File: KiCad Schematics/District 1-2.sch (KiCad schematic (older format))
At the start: 23 parts, among them M1 Fan

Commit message: Updated schematic
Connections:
- net labels removed: Programming_Track
- wire segments 138 -> 136
- no-connect marks 5 -> 7
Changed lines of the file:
@@
 $Descr USLetter 11000 8500
 encoding utf-8
-Sheet 5 6
+Sheet 5 7
 Title "District 1 Power Box"
 Date "2016-09-30"
@@
 	2020 4820 2020 4740
 Wire Wire Line
-	1360 4740 2020 4740
-Wire Wire Line
-	1360 3220 1360 4740
+	2020 4740 1360 4740
+Wire Wire Line
+	1360 4740 1360 3220
 Wire Wire Line
 	2020 6330 2020 6270
@@
 	5660 2010 5660 2560
 Wire Wire Line
-	2500 3490 2500 3160
-Wire Wire Line
-	2700 3160 2700 3490
-Wire Wire Line
 	2600 3490 2600 3230
 Wire Wire Line
 	2600 3230 1800 3230
 Connection ~ 1800 3230
-Entry Wire Line
-	2500 3160 2600 3060
-Entry Wire Line
-	2700 3160 2800 3060
-Text Label 3020 3060 0    60   ~ 0
-Programming_Track
-Wire Bus Line
-	2600 3060 3910 3060
+NoConn ~ 2700 3490
+NoConn ~ 2500 3490
 $EndSCHEMATC

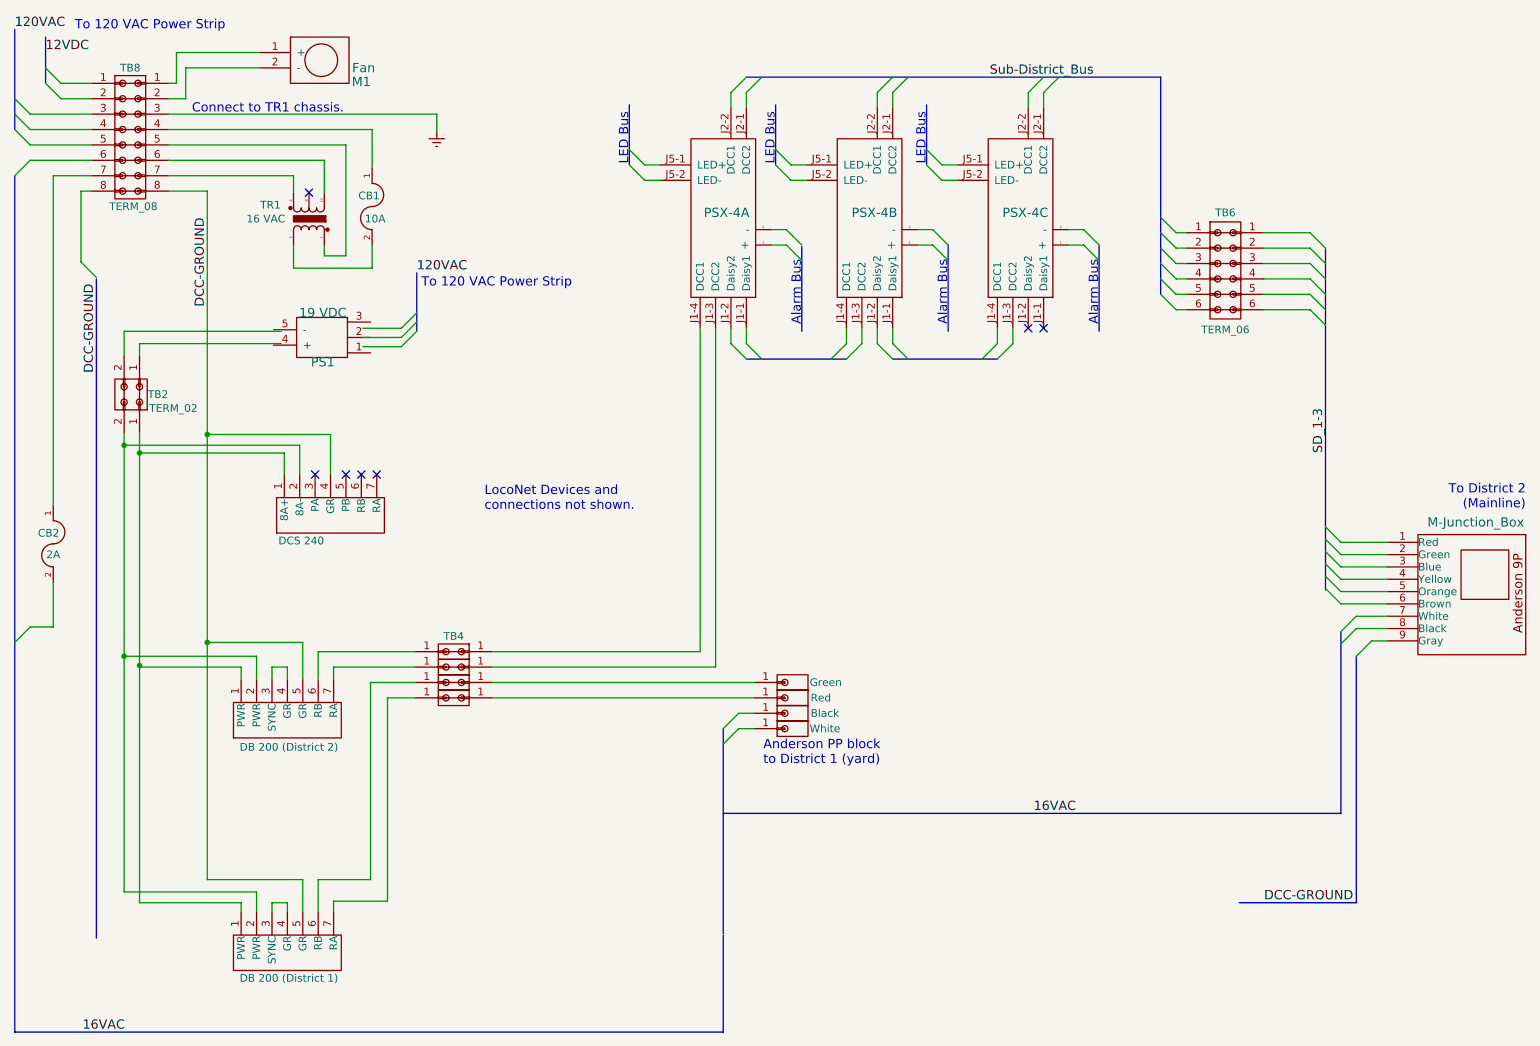
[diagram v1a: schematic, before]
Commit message: Simplified schematic
Added heirarchy sheets to simplify the schematic.
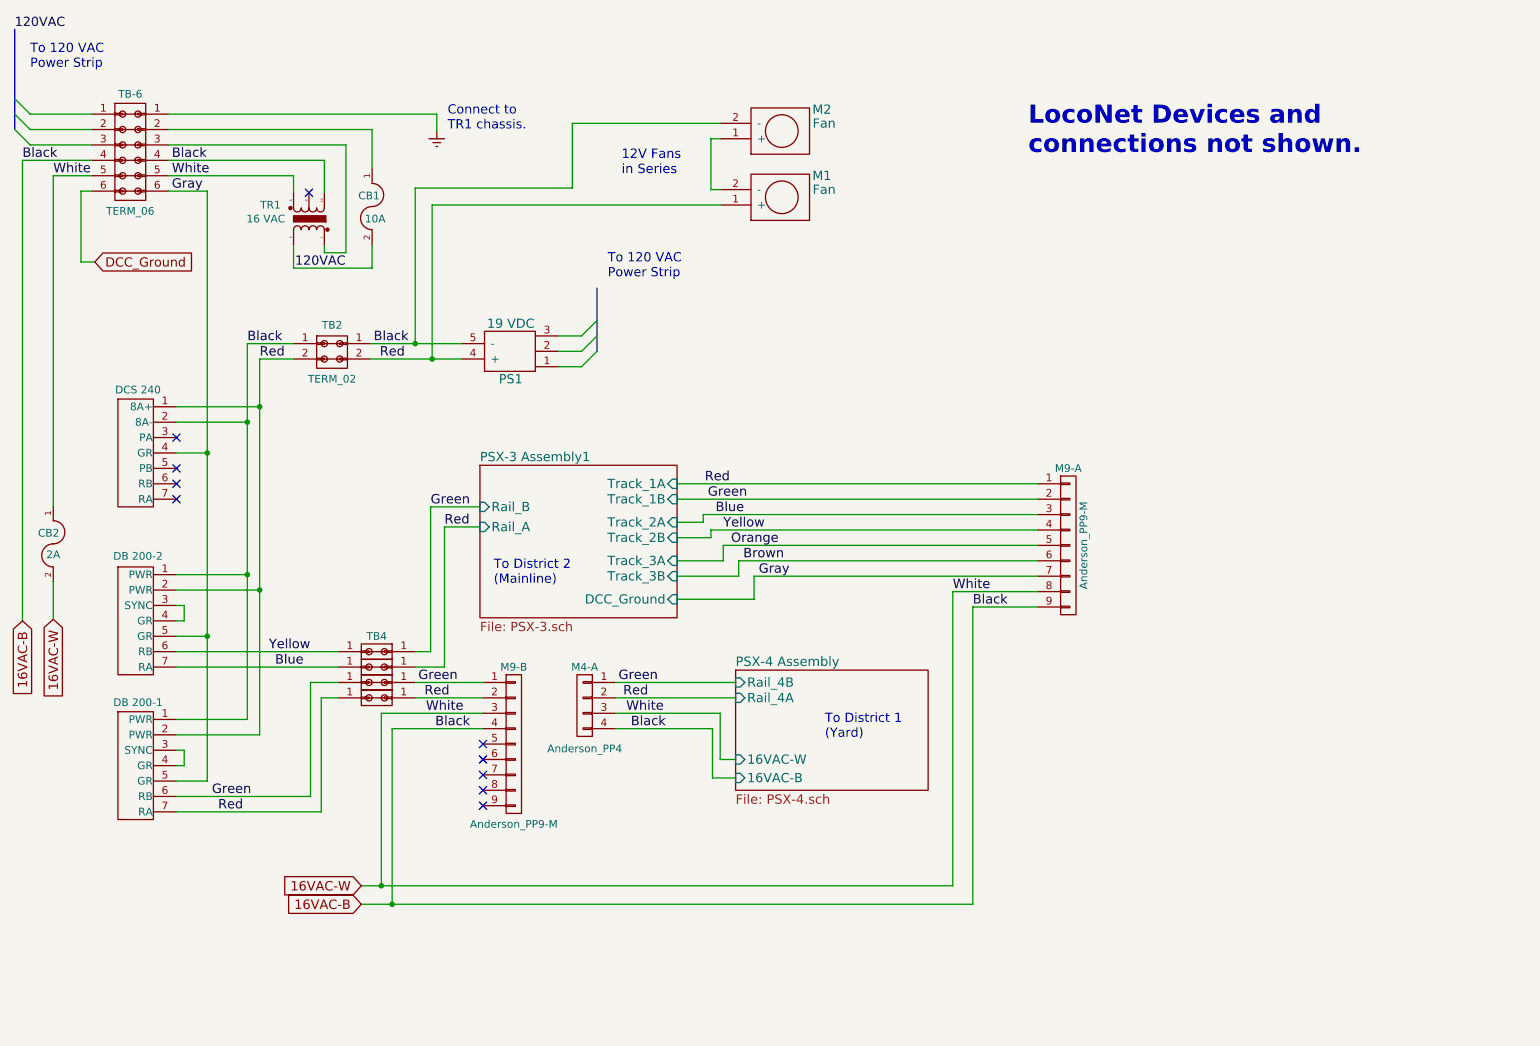
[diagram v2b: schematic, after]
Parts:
- removed M?: M-Junction_Box, symbol M-Junction_Box_No-Tap
- removed PSX?: PSX-4A, symbol PSX-4
- removed PSX?: PSX-4B, symbol PSX-4
- removed PSX?: PSX-4C, symbol PSX-4
- removed T?: Green, symbol CONN-1
- removed T?: Red, symbol CONN-1
- removed T?: Black, symbol CONN-1
- removed T?: White, symbol CONN-1
- removed TB6: TERM_06, symbol TERM_06
- removed TB8: TERM_08, symbol TERM_08
- added M2: Fan, symbol Fan
- added M4-A: Anderson_PP4, symbol CONN_01X04
- added M9-A, M9-B: Anderson_PP9-M, symbol CONN_01X09
- added TB-6: TERM_06, symbol TERM_06
- C2: value DB 200 (District 2) -> DB 200-2
- C3: value DB 200 (District 1) -> DB 200-1
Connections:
- net labels added: 16VAC-B, 16VAC-W, Black, Blue, Brown, DCC_Ground, Gray, Green, Orange, Red, White, Yellow
- net labels removed: 12VDC, 16VAC, DCC-GROUND, SD_1-3, Sub-District_Bus
- wire segments 136 -> 112
- no-connect marks 7 -> 10
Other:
- note added: "12V Fans\nin Series"
- note added: "Connect to\nTR1 chassis."
- note added: "To 120 VAC\nPower Strip"
- note added: "To District 1\n(Yard)"
- note removed: "Alarm Bus"
- note removed: "Anderson PP block\nto District 1 (yard)"
- note removed: "Connect to TR1 chassis."
- note removed: "LED Bus"
- note removed: "To 120 VAC Power Strip"
- moved on the sheet: M1, PS1, TB2

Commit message: Minor schematic changes
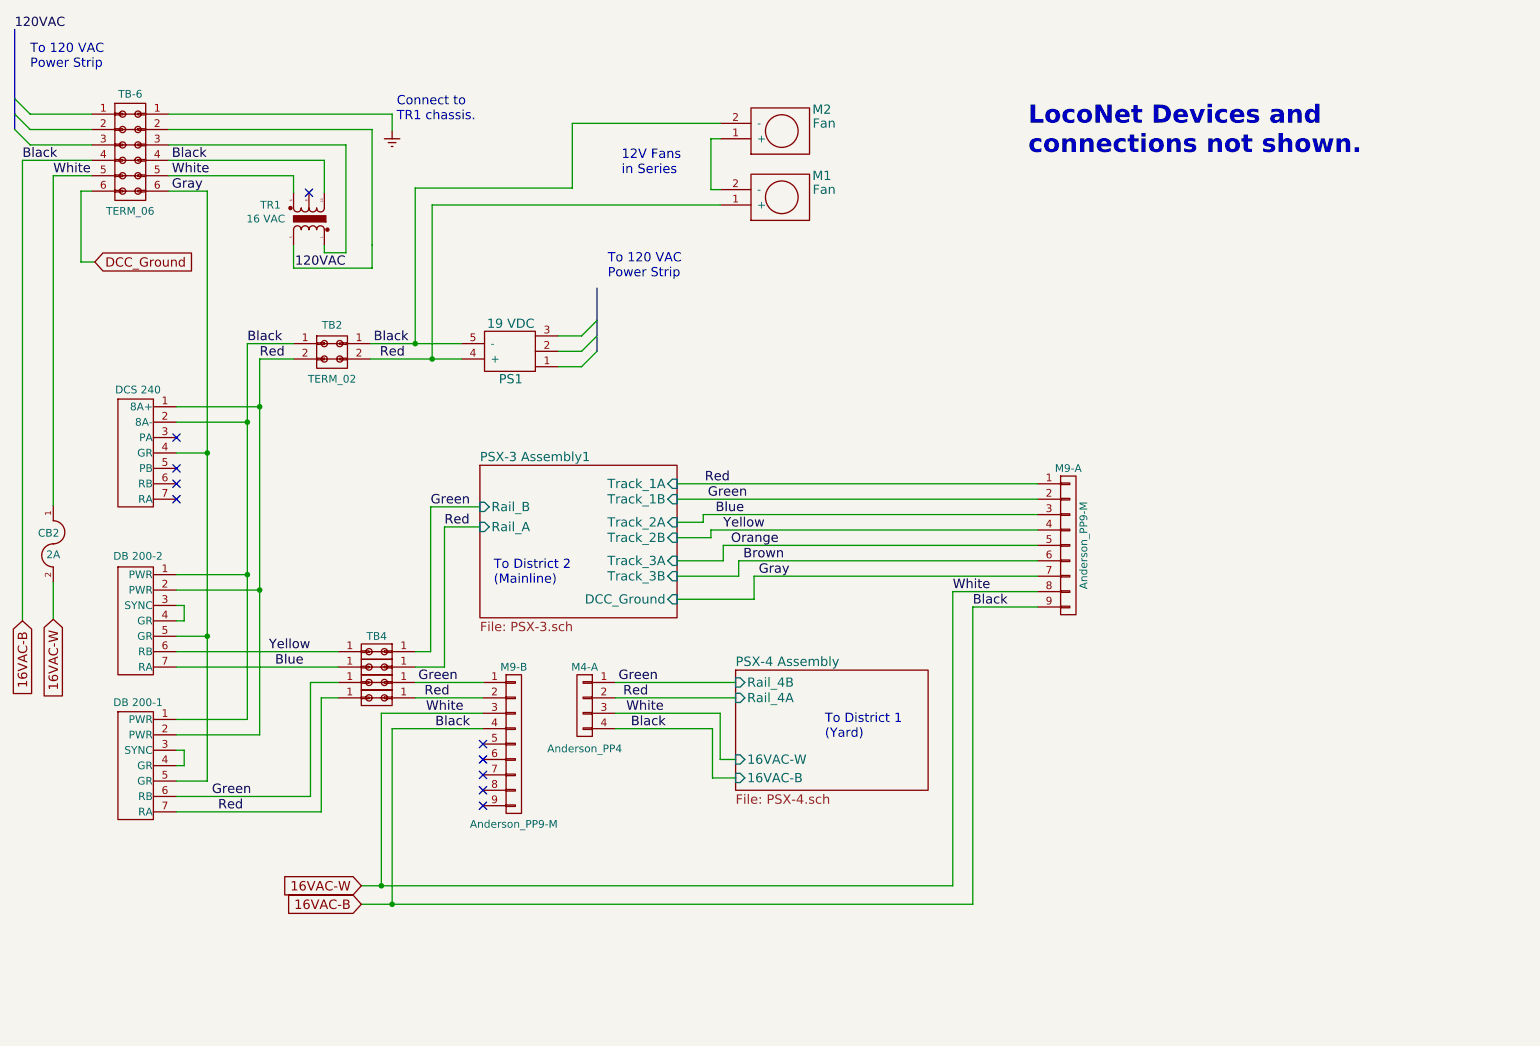
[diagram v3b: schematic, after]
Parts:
- removed CB1: 10A, symbol FUSE
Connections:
- net 120VAC: now also TB-6.2 (P2)
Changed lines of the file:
@@
 L Earth #PWR?
 U 1 1 57EBE4ED
-P 3290 1260
-F 0 "#PWR?" H 3290 1010 50  0001 C CNN
-F 1 "Earth" H 3290 1110 50  0001 C CNN
-F 2 "" H 3290 1260 50  0000 C CNN
-F 3 "" H 3290 1260 50  0000 C CNN
-	1    3290 1260
+P 3000 1260
+F 0 "#PWR?" H 3000 1010 50  0001 C CNN
+F 1 "Earth" H 3000 1110 50  0001 C CNN
+F 2 "" H 3000 1260 50  0000 C CNN
+F 3 "" H 3000 1260 50  0000 C CNN
+	1    3000 1260
 	1    0    0    -1
 $EndComp
@@
 	1050 1350 650  1350
 Wire Bus Line
-	550  600  550  1250
+	550  600  550  1050
+Wire Bus Line
+	550  1050 550  1150
+Wire Bus Line
+	550  1150 550  1250
 Wire Wire Line
 	1550 1450 2560 1450
@@
 	1550 1350 2700 1350
 Wire Wire Line
-	1550 1150 3290 1150
-Wire Wire Line
-	3290 1150 3290 1260
-Text Notes 3360 1260 0    60   ~ 0
+	1550 1150 3000 1150
+Wire Wire Line
+	3000 1150 3000 1260
+Text Notes 3030 1200 0    60   ~ 0
 Connect to\nTR1 chassis.
-$Comp
-L FUSE CB1
-U 1 1 57EBE4FE
-P 2870 1750
-F 0 "CB1" V 2800 1730 50  0000 C CNN
-F 1 "10A" V 2950 1770 50  0000 C CNN
-F 2 "" H 2870 1750 50  0000 C CNN
-F 3 "" H 2870 1750 50  0000 C CNN
-	1    2870 1750
-	0    1    1    0
-$EndComp
 Wire Wire Line
 	2870 2150 2870 2000
 Wire Wire Line
-	2870 1250 2870 1500
+	2870 1250 2870 2000
 Wire Wire Line
 	2700 1350 2700 2050
@@
 	4230 2790 4330 2690
 Wire Bus Line
-	4330 2280 4330 2590
+	4330 2280 4330 2490
+Wire Bus Line
+	4330 2490 4330 2590
 Wire Bus Line
 	4330 2600 4330 2690
@@
 	1800 1650 1550 1650
 Wire Wire Line
-	2860 2640 3450 2640
-Wire Wire Line
-	2860 2740 3450 2740
+	2860 2640 3150 2640
+Wire Wire Line
+	3150 2640 3450 2640
+Wire Wire Line
+	2860 2740 3260 2740
+Wire Wire Line
+	3260 2740 3450 2740
 Wire Wire Line
 	2360 2740 2140 2740
 Wire Wire Line
-	2140 2740 2140 5180
+	2140 2740 2140 3050
+Wire Wire Line
+	2140 3050 2140 4240
+Wire Wire Line
+	2140 4240 2140 5180
 Wire Wire Line
 	2140 3050 1600 3050
@@
 	2360 2640 2060 2640
 Wire Wire Line
-	2060 2640 2060 5080
+	2060 2640 2060 3150
+Wire Wire Line
+	2060 3150 2060 4140
+Wire Wire Line
+	2060 4140 2060 5080
 Wire Wire Line
 	2060 3150 1600 3150
 Wire Wire Line
-	1800 1650 1800 5480
+	1800 1650 1800 3350
+Wire Wire Line
+	1800 3350 1800 4540
+Wire Wire Line
+	1800 4540 1800 5480
 Wire Wire Line
 	1800 3350 1600 3350
@@
 	2930 5040 2930 6160
 Wire Wire Line
-	2800 6160 6640 6160
-Wire Wire Line
-	2800 6280 6770 6280
+	2800 6160 2930 6160
+Wire Wire Line
+	2930 6160 6640 6160
+Wire Wire Line
+	2800 6280 3000 6280
+Wire Wire Line
+	3000 6280 6770 6280
 Wire Wire Line
 	3000 6280 3000 5140

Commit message: Updated schematic (reverted)
Reverted back to the correct wiring as the boards were rewired to spec.
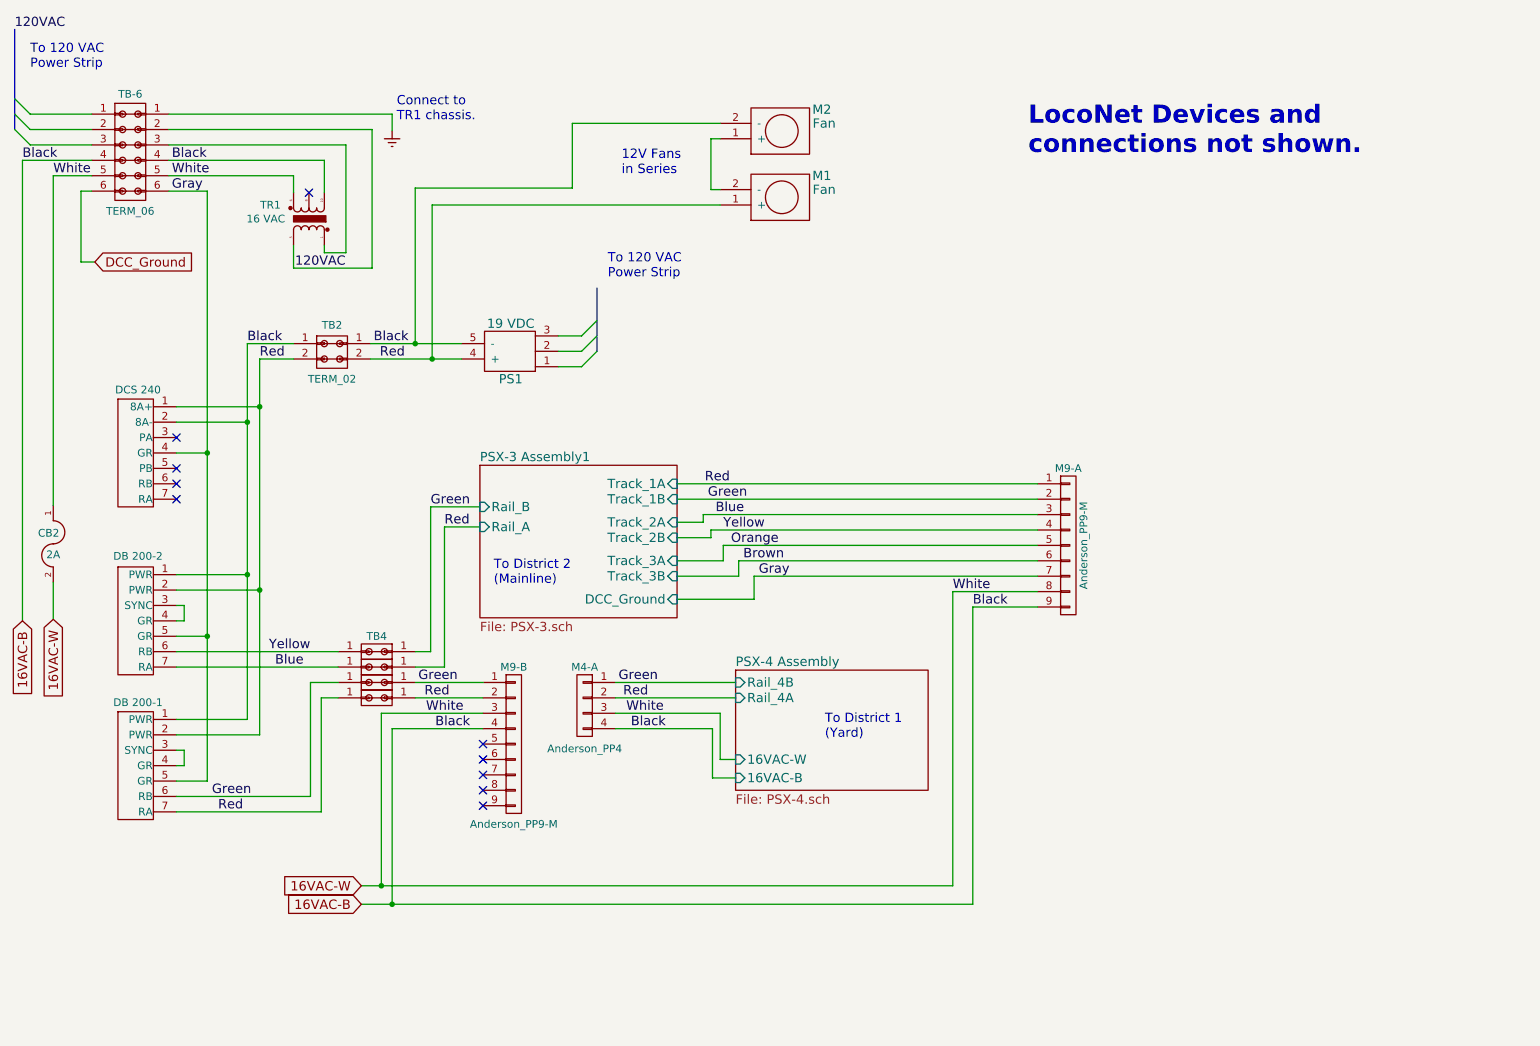
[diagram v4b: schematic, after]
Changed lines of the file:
@@
 	1050 1350 650  1350
 Wire Bus Line
-	550  600  550  1050
-Wire Bus Line
-	550  1050 550  1150
-Wire Bus Line
-	550  1150 550  1250
+	550  600  550  1250
 Wire Wire Line
 	1550 1450 2560 1450
@@
 	2360 2000 2360 2150
 Wire Wire Line
-	2360 2150 2870 2150
+	2870 2150 2360 2150
 Wire Wire Line
 	1550 1250 2870 1250
@@
 Connect to\nTR1 chassis.
 Wire Wire Line
-	2870 2150 2870 2000
-Wire Wire Line
-	2870 1250 2870 2000
+	2870 1250 2870 2150
 Wire Wire Line
 	2700 1350 2700 2050
@@
 	4230 2790 4330 2690
 Wire Bus Line
-	4330 2280 4330 2490
-Wire Bus Line
-	4330 2490 4330 2590
+	4330 2280 4330 2590
 Wire Bus Line
 	4330 2600 4330 2690
@@
 	1800 1650 1550 1650
 Wire Wire Line
-	2860 2640 3150 2640
-Wire Wire Line
-	3150 2640 3450 2640
-Wire Wire Line
-	2860 2740 3260 2740
-Wire Wire Line
-	3260 2740 3450 2740
+	2860 2640 3450 2640
+Wire Wire Line
+	2860 2740 3450 2740
 Wire Wire Line
 	2360 2740 2140 2740
 Wire Wire Line
-	2140 2740 2140 3050
-Wire Wire Line
-	2140 3050 2140 4240
-Wire Wire Line
-	2140 4240 2140 5180
+	2140 2740 2140 5180
 Wire Wire Line
 	2140 3050 1600 3050
@@
 	2360 2640 2060 2640
 Wire Wire Line
-	2060 2640 2060 3150
-Wire Wire Line
-	2060 3150 2060 4140
-Wire Wire Line
-	2060 4140 2060 5080
+	2060 2640 2060 5080
 Wire Wire Line
 	2060 3150 1600 3150
 Wire Wire Line
-	1800 1650 1800 3350
-Wire Wire Line
-	1800 3350 1800 4540
-Wire Wire Line
-	1800 4540 1800 5480
+	1800 1650 1800 5480
 Wire Wire Line
 	1800 3350 1600 3350
@@
 	2930 5040 2930 6160
 Wire Wire Line
-	2800 6160 2930 6160
-Wire Wire Line
-	2930 6160 6640 6160
-Wire Wire Line
-	2800 6280 3000 6280
-Wire Wire Line
-	3000 6280 6770 6280
+	2800 6160 6640 6160
+Wire Wire Line
+	2800 6280 6770 6280
 Wire Wire Line
 	3000 6280 3000 5140
